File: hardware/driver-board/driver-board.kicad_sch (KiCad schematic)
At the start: 29 parts, among them J1 Conn_ARM_JTAG_SWD_10, J2 USB_C_Receptacle_USB2.0_16P, SW1 SW_Push, U1 STM32F103CBT6, U2 USBLC6-2SC6, Y1 16Mhz

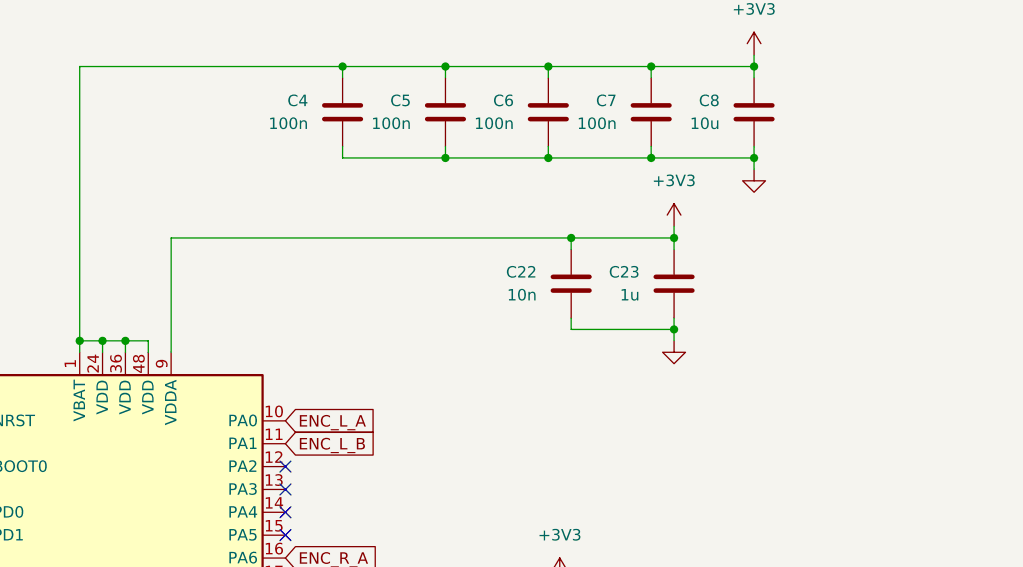
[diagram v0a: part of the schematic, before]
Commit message: Add VDDA supply filter
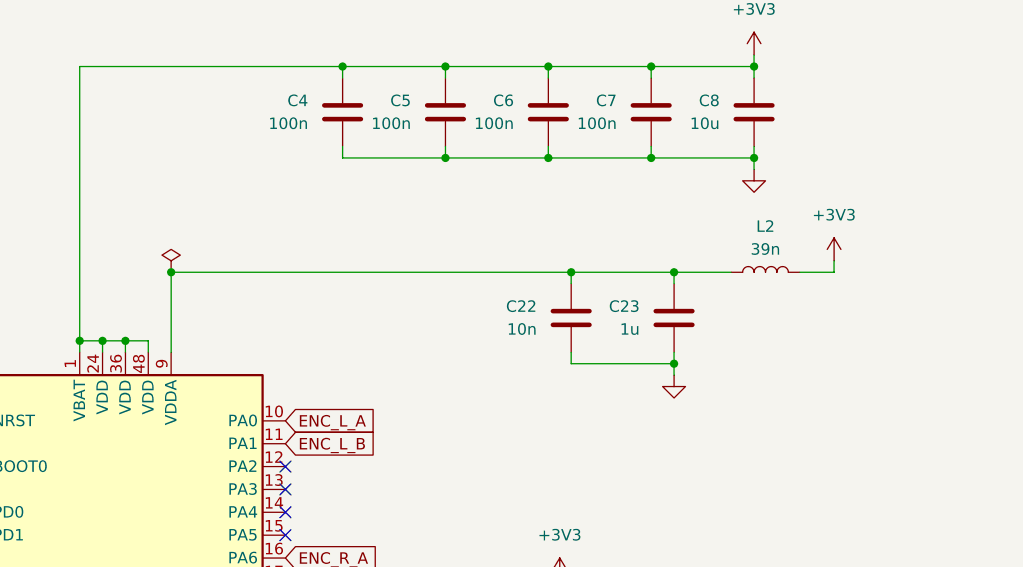
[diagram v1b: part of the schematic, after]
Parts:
- added L2: 39n, Inductor_SMD:L_0402_1005Metric, symbol Device:L
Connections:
- net +3V3: now also L2.2; no longer C22.1, C23.1, U1.9 (VDDA)
- new net: C22.1, C23.1, L2.1, U1.9 (VDDA)
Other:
- moved on the sheet: C22, C23

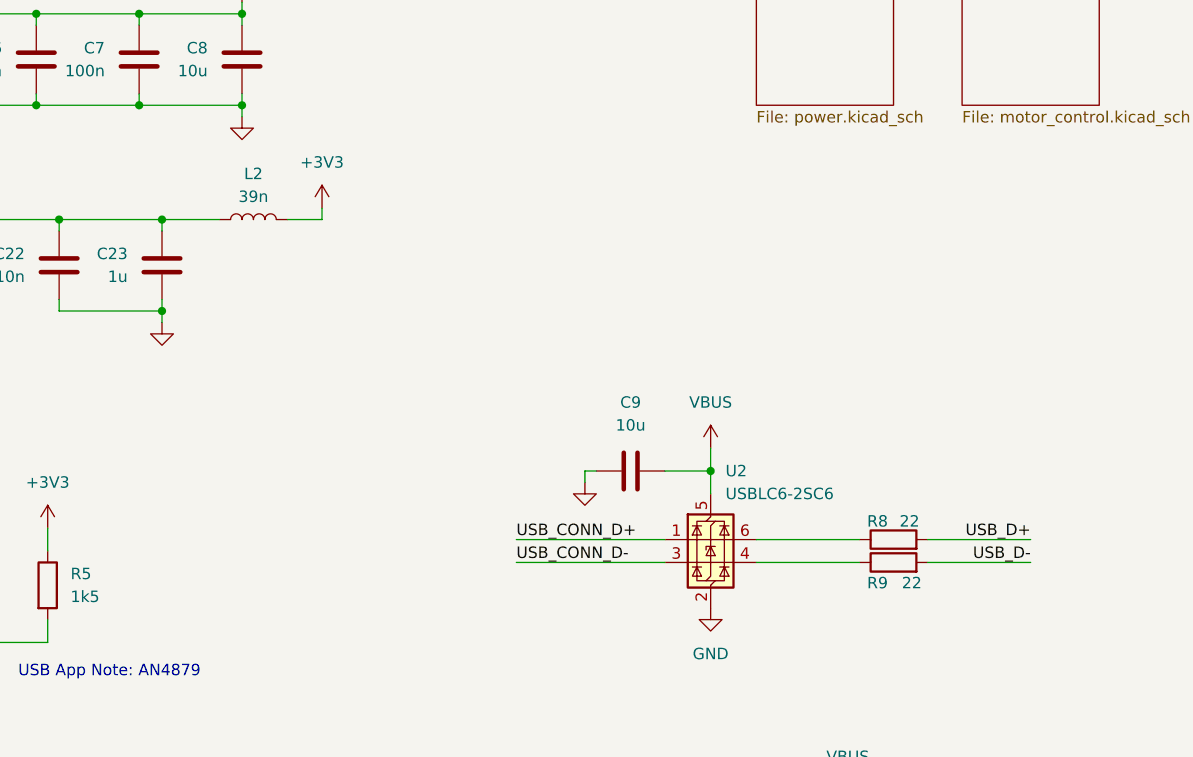
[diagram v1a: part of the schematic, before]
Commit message: Update driver board USB-C and power circuitry
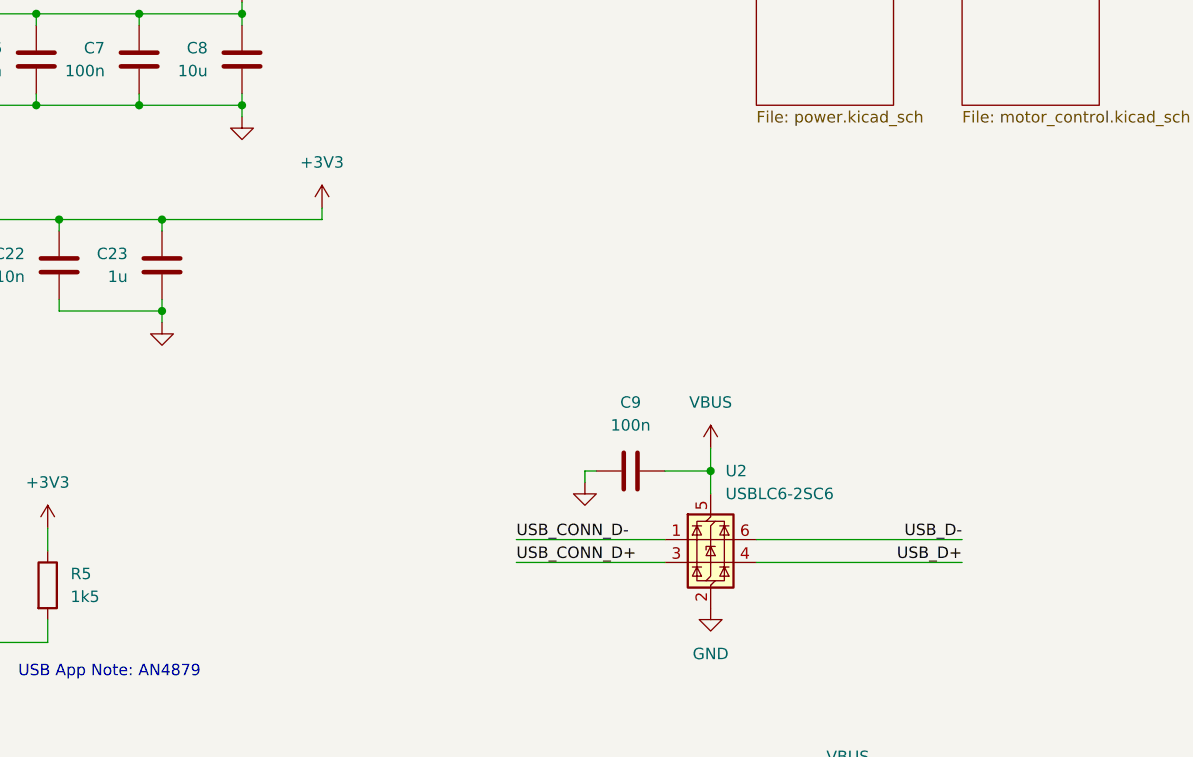
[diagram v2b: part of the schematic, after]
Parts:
- removed L2: 39n, Inductor_SMD:L_0402_1005Metric, symbol Device:L
- removed R8, R9: 22, Resistor_SMD:R_0402_1005Metric, symbol Device:R
- C9: value 10u -> 100n; footprint Capacitor_SMD:C_0805_2012Metric -> Capacitor_SMD:C_0402_1005Metric; JLCPCB C15850 -> C307331
- J2: footprint Connector_USB:USB_C_Receptacle_G-Switch_GT-USB-7025 -> Connector_USB:USB_C_Receptacle_G-Switch_GT-USB-7010ASV; JLCPCB C963213 -> C2988369
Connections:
- net +3V3: now also C22.1, C23.1, U1.9 (VDDA)
- net GND: now also C9.2; no longer C9.1
- net USB_CONN_D+: now also U2.3 (I/O2); no longer U2.1 (I/O1)
- net USB_CONN_D-: now also U2.1 (I/O1); no longer U2.3 (I/O2)
- net USB_D+: now also U2.4 (I/O2)
- net USB_D-: now also U2.6 (I/O1)
- net VBUS: now also C9.1; no longer C9.2

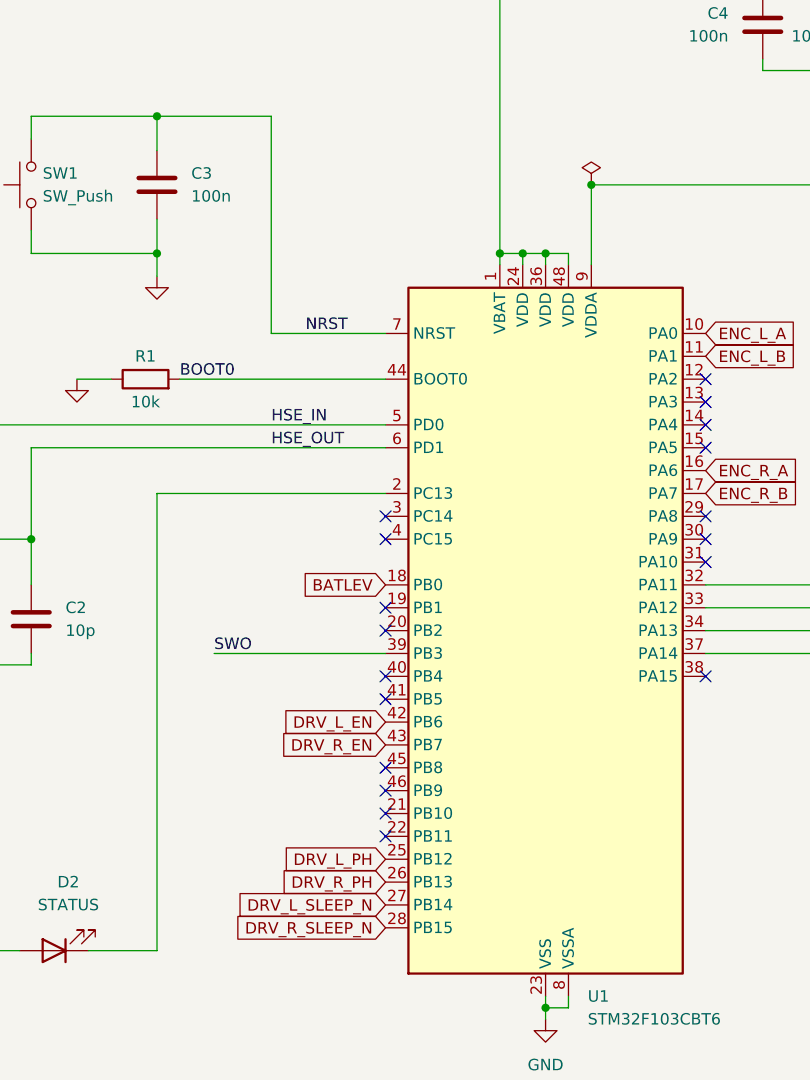
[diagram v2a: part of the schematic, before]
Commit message: Refine driver board layout and 3D models
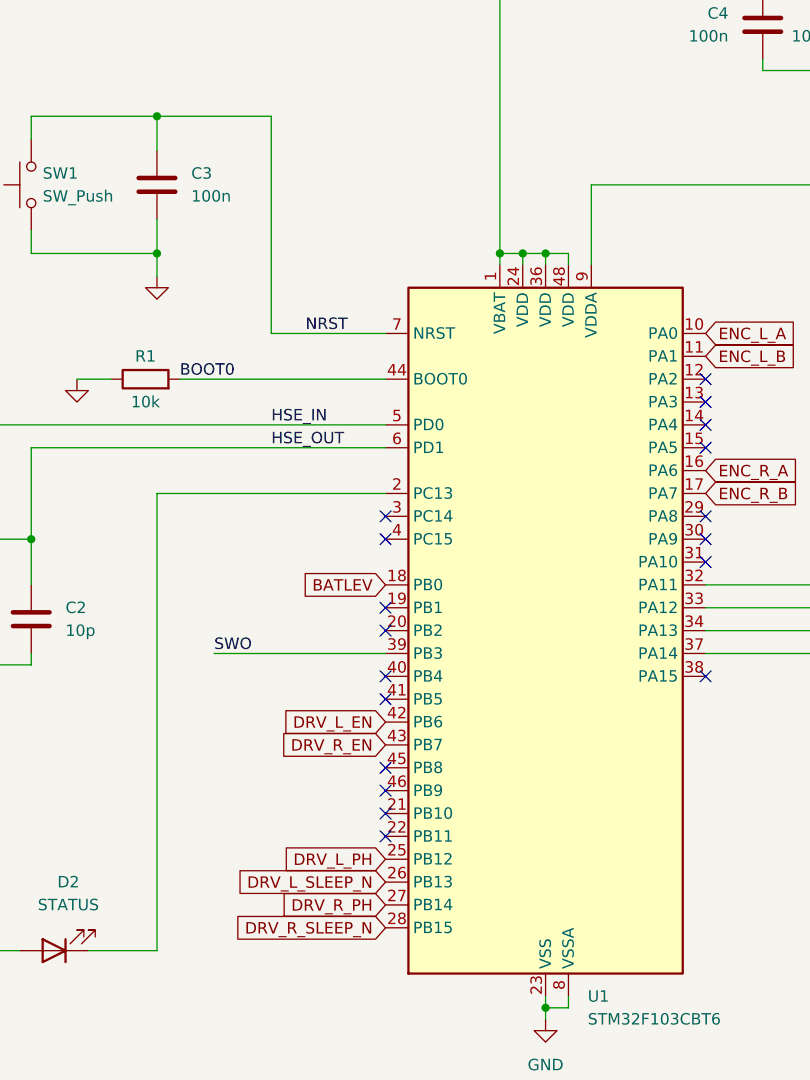
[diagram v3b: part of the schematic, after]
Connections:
- net DRV_L_SLEEP_N: now also U1.26 (PB13); no longer U1.27 (PB14)
- net DRV_R_PH: now also U1.27 (PB14); no longer U1.26 (PB13)
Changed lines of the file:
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@@
 	)
 	(junction
-		(at 109.22 45.72)
-		(diameter 0)
-		(color 0 0 0 0)
-	)
-	(junction
 		(at 165.1 45.72)
 		(diameter 0)
@@
 	)
 	(no_connect
+		(at 86.36 102.87)
+	)
+	(no_connect
 		(at 121.92 67.31)
 	)
@@
 	)
 	(no_connect
+		(at 86.36 100.33)
+	)
+	(no_connect
 		(at 86.36 113.03)
 	)
@@
 	)
 	(no_connect
-		(at 86.36 100.33)
-	)
-	(no_connect
 		(at 86.36 95.25)
 	)
@@
 	)
 	(no_connect
-		(at 86.36 102.87)
-	)
-	(no_connect
 		(at 121.92 85.09)
 	)
@@
 		)
 	)
-	(global_label "DRV_R_PH"
+	(global_label "DRV_L_SLEEP_N"
 		(shape input)
 		(at 86.36 123.19 180)
@@
 		)
 	)
-	(global_label "DRV_L_SLEEP_N"
+	(global_label "DRV_R_PH"
 		(shape input)
 		(at 86.36 125.73 180)
@@
 					(unit 1)
 				)
-			)
-		)
-	)
-	(symbol
-		(lib_id "PCM_4ms_Power-symbol:PWR_FLAG")
-		(at 109.22 45.72 0)
-		(unit 1)
-		(body_style 1)
-		(exclude_from_sim no)
-		(in_bom yes)
-		(on_board yes)
-		(in_pos_files yes)
-		(dnp no)
-		(fields_autoplaced yes)
-		(property "Reference" "#FLG07"
-			(at 109.22 47.625 0)
-			(hide yes)
-			(show_name no)
-			(do_not_autoplace no)
-			(effects
-				(font
-					(size 1.27 1.27)
-				)
-			)
-		)
-		(property "Value" "PWR_FLAG"
-			(at 109.22 49.53 0)
-			(hide yes)
-			(show_name no)
-			(do_not_autoplace no)
-			(effects
-				(font
-					(size 1.27 1.27)
-				)
-			)
-		)
-		(property "Footprint" ""
-			(at 109.22 45.72 0)
-			(hide yes)
-			(show_name no)
-			(do_not_autoplace no)
-			(effects
-				(font
-					(size 1.27 1.27)
-				)
-			)
-		)
-		(property "Datasheet" ""
-			(at 109.22 45.72 0)
-			(hide yes)
-			(show_name no)
-			(do_not_autoplace no)
-			(effects
-				(font
-					(size 1.27 1.27)
-				)
-			)
-		)
-		(property "Description" ""
-			(at 109.22 45.72 0)
-			(hide yes)
-			(show_name no)
-			(do_not_autoplace no)
-			(effects
-				(font
-					(size 1.27 1.27)
-				)
-			)
-		)
-		(pin "1"
-		)
-		(instances
-			(project "driver-board"
-				(path "/3304d5f8-08d9-4046-829b-96d64a4f111d"
-					(reference "#FLG07")
-					(unit 1)
-				)
